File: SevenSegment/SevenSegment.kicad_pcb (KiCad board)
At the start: 2 copper layers, 28.5 x 42.7 mm, 11 parts, among them IC1 CD4033BE, IC2 CD4033BE, J1 Conn_01x04

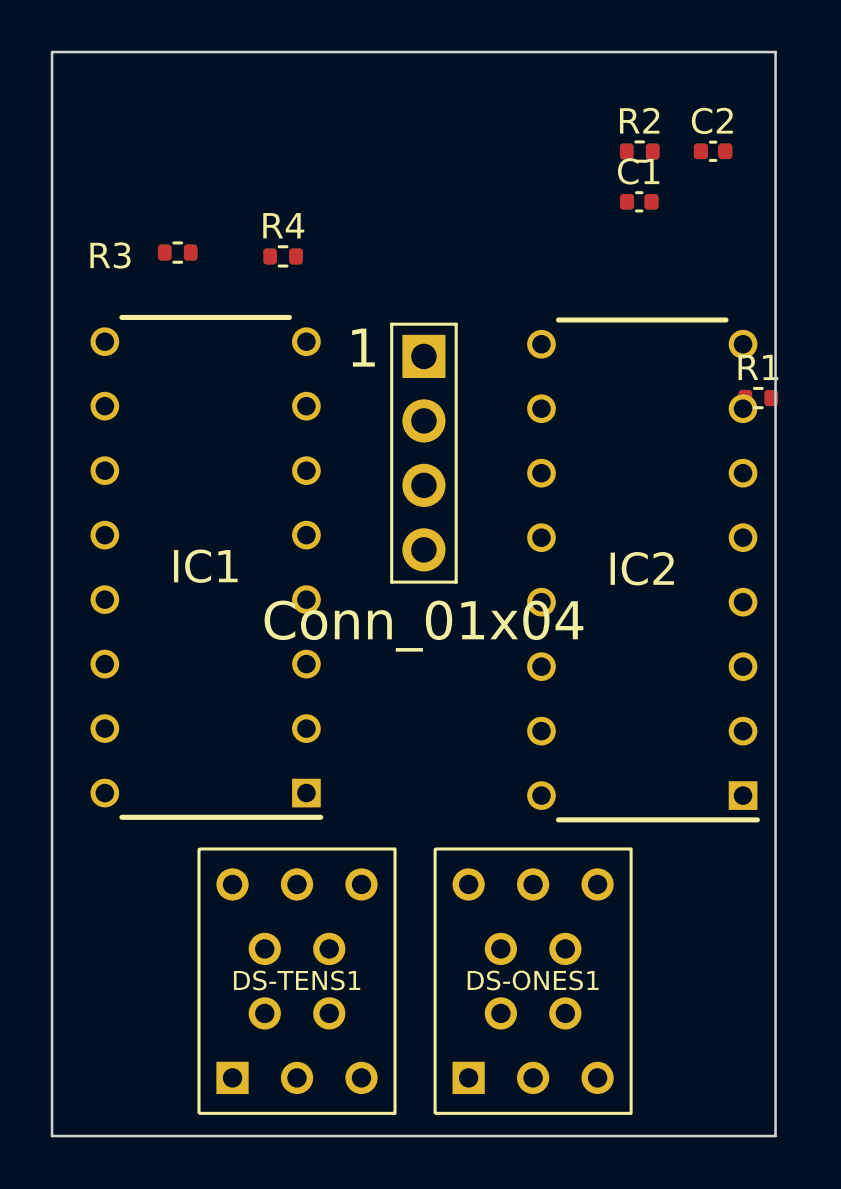
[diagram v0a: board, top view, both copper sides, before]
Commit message: Layout SevenSegment Board. Nano Schematic
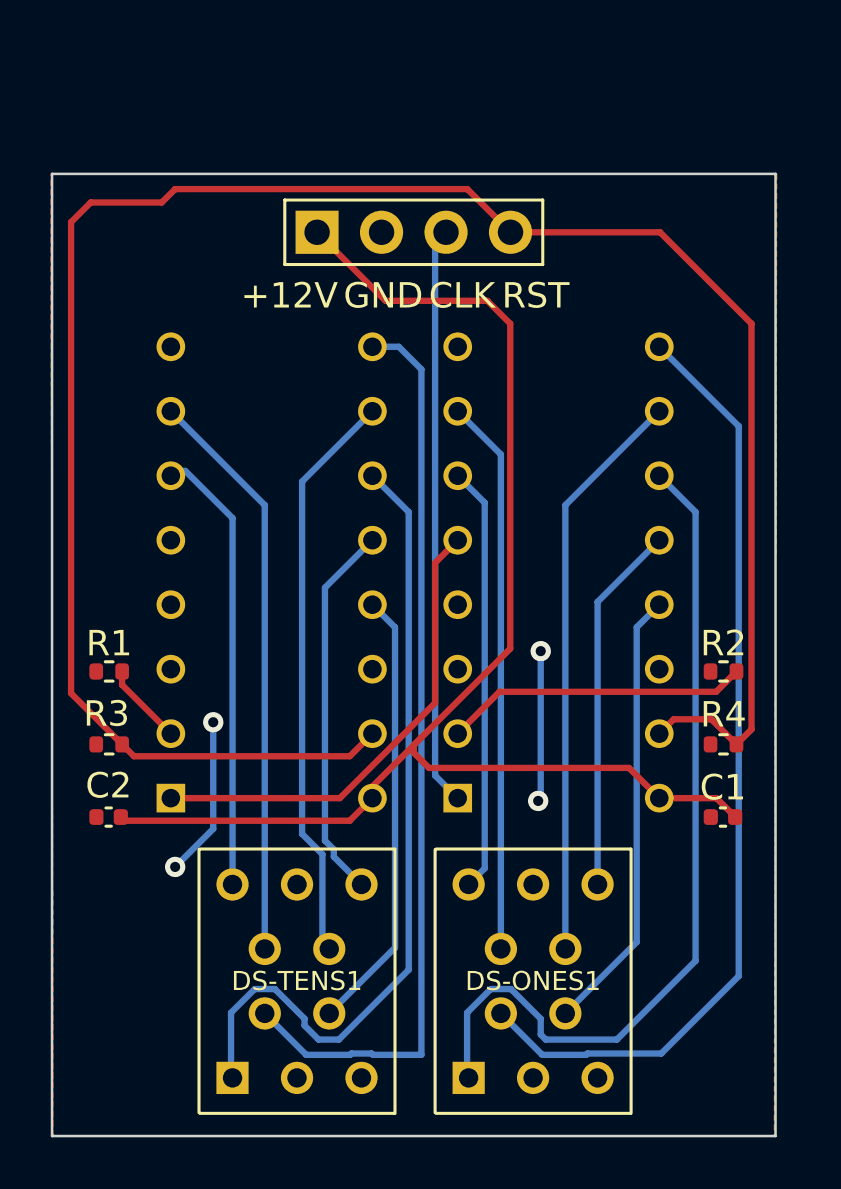
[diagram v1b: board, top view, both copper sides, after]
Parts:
- IC1, IC2: moved to B.Cu
- moved C2 35.4 mm to (92.2, 102.3)
- moved R1 27.7 mm to (92.2, 96.6), turned to 180 degrees
- moved R4 25.9 mm to (116.4, 99.5)
- moved C1 24.5 mm to (116.4, 102.3)
- moved R2 20.7 mm to (116.4, 96.6), turned to 180 degrees
- moved R3 19.6 mm to (92.2, 99.5)
- moved J1 8.71 mm to (104.2, 79.3), turned to 90 degrees
- moved IC2 3.30 mm to (109.9, 92.7), turned to 0 degrees
- moved IC1 2.61 mm to (98.6, 92.7), turned to 0 degrees
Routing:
- net /RESET: track 0.00 -> 81.9 mm
- net +12V: track 0.00 -> 54.7 mm
- net /D1: track 0.00 -> 37.4 mm
- net /D2: track 0.00 -> 36.2 mm
- net /E1: track 0.00 -> 34.3 mm
- net /E2: track 0.00 -> 32.3 mm
- net CLOCK_BAR: track 0.00 -> 22.8 mm
- net /A2: track 0.00 -> 22.8 mm
- net /G2: track 0.00 -> 22.7 mm
- net /A1: track 0.00 -> 22.7 mm
- net /G1: track 0.00 -> 21.9 mm
- net CARRY_1: track 0.00 -> 18.7 mm
- net /F2: track 0.00 -> 17.7 mm
- net /C1: track 0.00 -> 17.6 mm
- net /C2: track 0.00 -> 17.5 mm
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- added copper zone on F.Cu, net GND
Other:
- board size 28.5 x 42.7 mm -> 28.5 x 37.9 mm
- board text added: "+12V"
- board text added: "CLK"
- board text added: "GND"
- board text added: "RST"
- board text added: "SevenSegment v0.0"

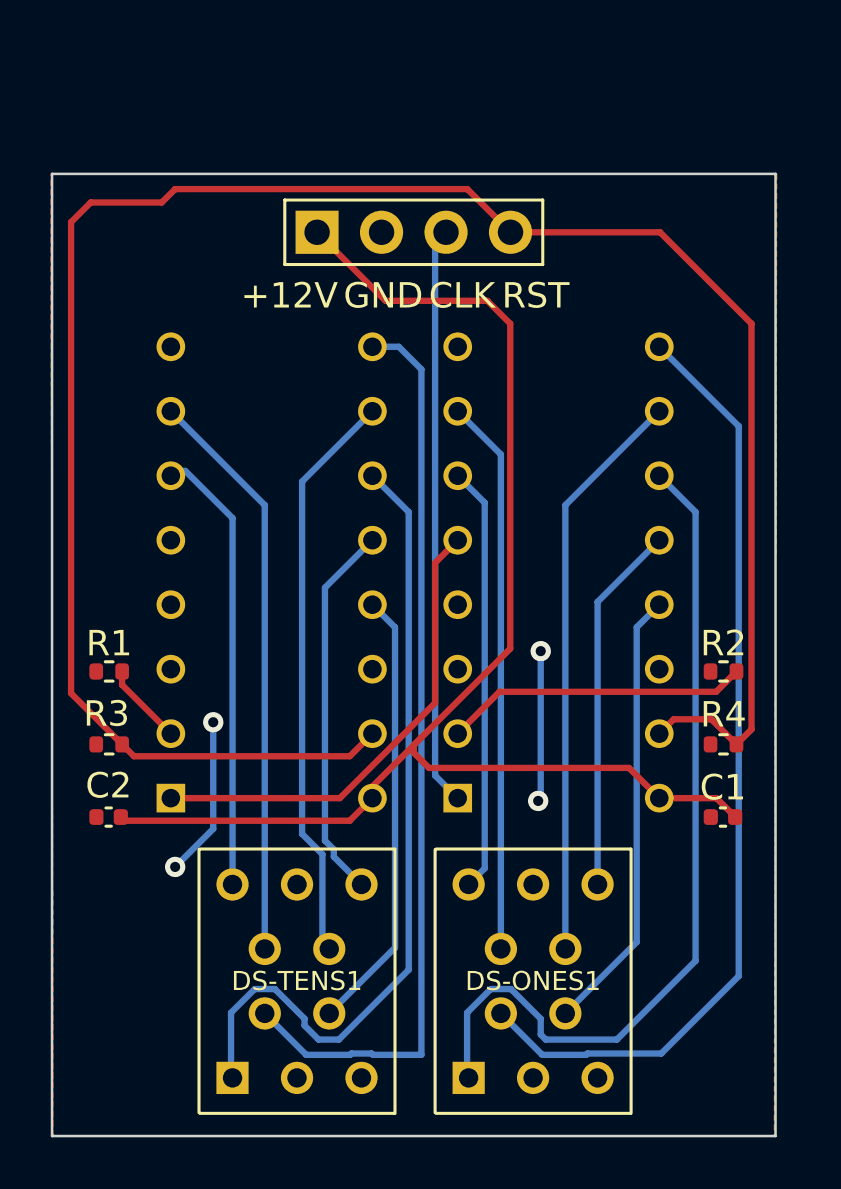
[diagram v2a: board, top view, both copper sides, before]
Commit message: SevenSegment PCB v1.0
Push TDSR0706's together, move header pins, add more header pins for mechanical stability, make board less wide, rounded tracks, moved ICs to top of board for better clearance.
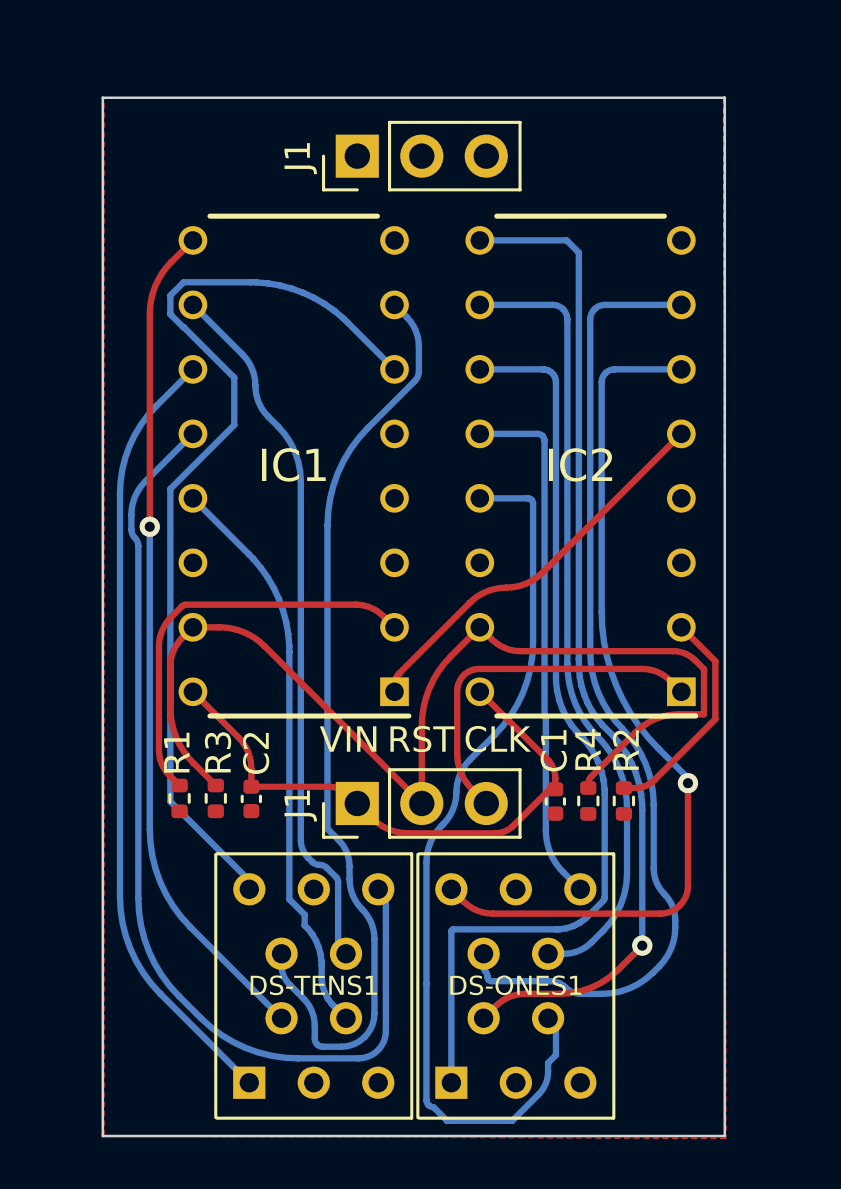
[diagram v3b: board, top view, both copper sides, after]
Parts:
- added J1: Conn_01x04, Connector_PinHeader_2.54mm:PinHeader_1x03_P2.54mm_Vertical, F.Cu at (102.0, 76.3)
- IC1, IC2: moved to F.Cu
- J1: footprint 4ms_Connector:Pins_1x04_2.54mm_TH_SWD -> Connector_PinHeader_2.54mm:PinHeader_1x03_P2.54mm_Vertical
- moved J1 22.6 mm to (102.0, 101.8)
- moved C1 6.63 mm to (109.8, 101.7), turned to 90 degrees
- moved R2 6.44 mm to (112.5, 101.7), turned to -90 degrees
- moved R4 5.77 mm to (111.1, 101.7), turned to 90 degrees
- moved R1 5.72 mm to (95.0, 101.6), turned to -90 degrees
- moved C2 5.67 mm to (97.8, 101.6), turned to 90 degrees
- moved R3 4.71 mm to (96.4, 101.6), turned to 90 degrees
- moved IC1 4.28 mm to (99.5, 88.5), turned to 180 degrees
- moved IC2 4.28 mm to (110.8, 88.5), turned to 180 degrees
- moved DS-ONES1 0.71 mm to (110.8, 105.2)
- moved DS-TENS1 0.69 mm to (102.8, 105.2)
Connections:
- J1 pad 2: GND -> /RESET
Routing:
- net /RESET: track 81.9 -> 43.6 mm
- net +12V: track 54.7 -> 22.8 mm
- net /B2: track 14.9 -> 38.7 mm
- net /F2: track 17.7 -> 37.0 mm
- net /C1: track 17.6 -> 35.5 mm
- net /F1: track 16.8 -> 34.5 mm, vias 0 -> 1
- net /G1: track 21.9 -> 38.6 mm
- net /G2: track 22.7 -> 37.0 mm
- net Net-(IC1-Pad2): track 3.25 -> 16.3 mm
- net GND: track 12.3 -> 0.00 mm, vias 4 -> 0
- net /A1: track 22.7 -> 31.1 mm
- net CLOCK_BAR: track 22.8 -> 14.4 mm
- net /B1: track 14.6 -> 20.8 mm
- net /A2: track 22.8 -> 27.8 mm
- net /C2: track 17.5 -> 22.6 mm
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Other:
- board size 28.5 x 37.9 mm -> 24.5 x 40.9 mm
- board text added: "SevenSegment v1.0"
- board text added: "VIN"
- board text removed: "+12V"
- board text removed: "GND"
- board text removed: "SevenSegment v0.0"

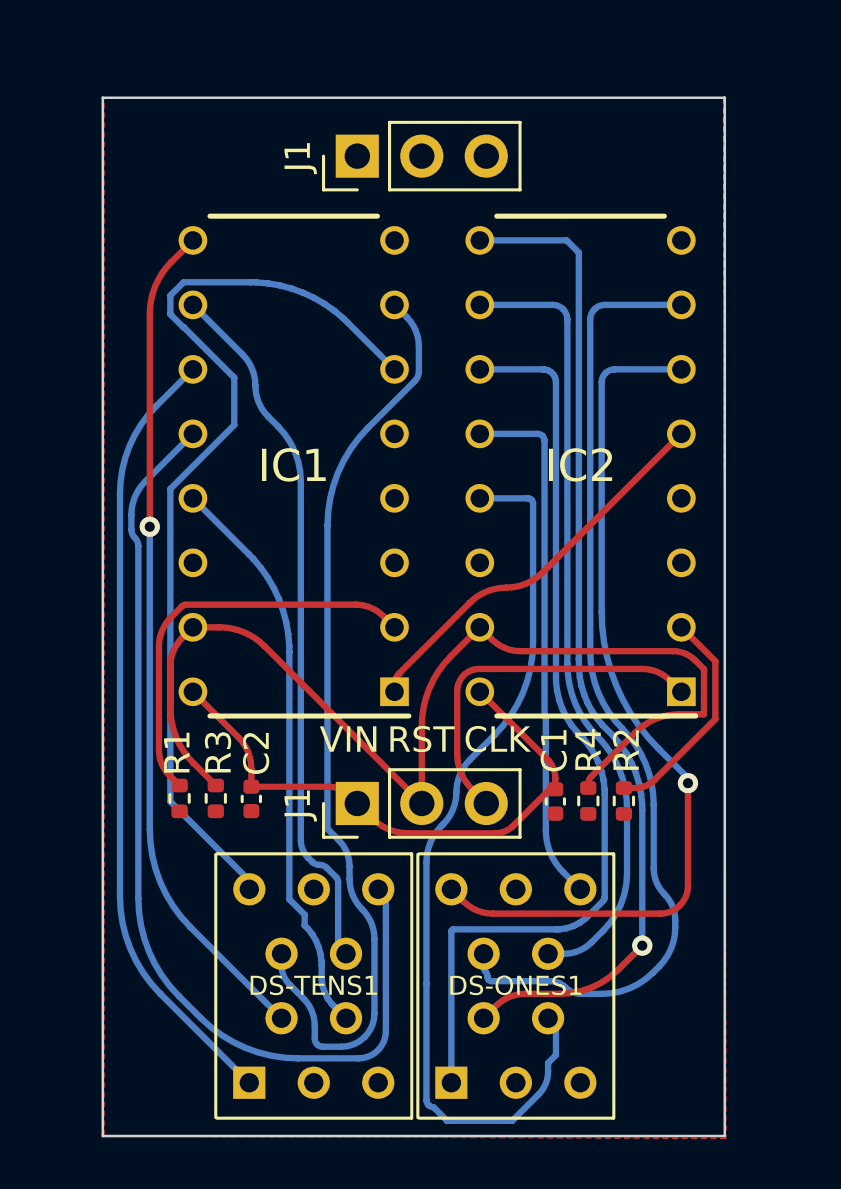
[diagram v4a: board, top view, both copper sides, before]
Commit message: Add startup led flashing to firmware.
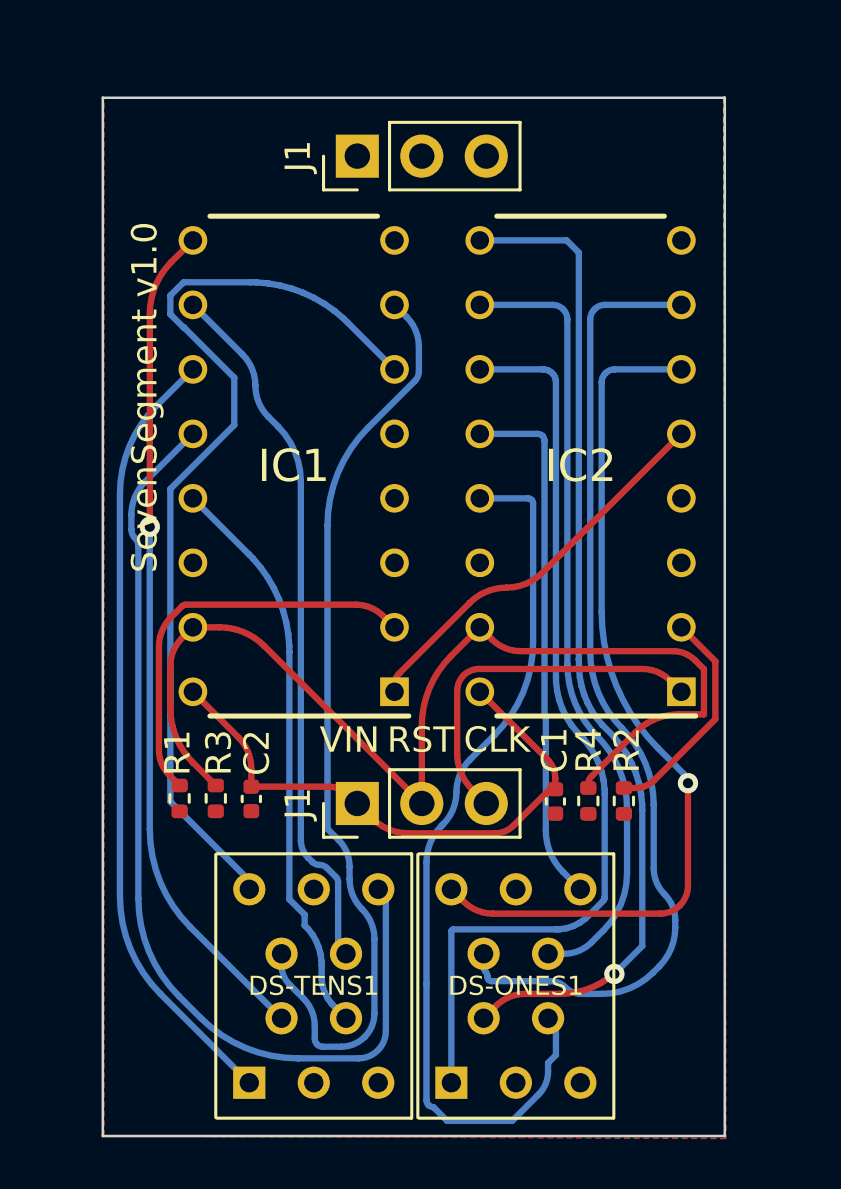
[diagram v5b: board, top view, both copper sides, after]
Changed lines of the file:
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@@
   (gr_rect (start 92 74) (end 116.5 114.9)
     (stroke (width 0.15) (type default)) (fill none) (layer "User.4"))
-  (gr_text "SevenSegment v1.0" (at 93.6 85.8 -270) (layer "B.SilkS")
-    (effects (font (size 1 1) (thickness 0.15)))
-  )
   (gr_text "RST\n" (at 104.475 99.3) (layer "F.SilkS")
     (effects (font (size 1 1) (thickness 0.15)))
@@
   )
   (gr_text "CLK" (at 107.475 99.3) (layer "F.SilkS")
+    (effects (font (size 1 1) (thickness 0.15)))
+  )
+  (gr_text "SevenSegment v1.0" (at 93.6 85.8 90) (layer "F.SilkS")
     (effects (font (size 1 1) (thickness 0.15)))
   )
@@
   (arc (start 110.183604 109.05) (mid 110.460516 109.235027) (end 110.787157 109.3) (width 0.25) (layer "B.Cu") (net 21))
   (arc (start 113.65 104.348959) (mid 113.760453 104.904248) (end 114.075 105.375) (width 0.25) (layer "B.Cu") (net 21))
-  (segment (start 113.2 107.4) (end 112.25 108.35) (width 0.25) (layer "F.Cu") (net 22))
-  (segment (start 109.956497 109.3) (end 108.588822 109.3) (width 0.25) (layer "F.Cu") (net 22))
+  (segment (start 112.102002 108.515408) (end 112.023617 108.515408) (width 0.25) (layer "F.Cu") (net 22))
+  (segment (start 112.023617 108.515408) (end 111.835011 108.704014) (width 0.25) (layer "F.Cu") (net 22))
   (segment (start 107.43 109.78) (end 106.95 110.26) (width 0.25) (layer "F.Cu") (net 22))
-  (via (at 113.2 107.4) (size 0.8) (drill 0.4) (layers "F.Cu" "B.Cu") (net 22))
+  (segment (start 109.951813 109.3) (end 108.588822 109.3) (width 0.25) (layer "F.Cu") (net 22))
+  (via (at 112.102002 108.515408) (size 0.8) (drill 0.4) (layers "F.Cu" "B.Cu") (net 22))
+  (arc (start 111.835011 108.704014) (mid 110.939505 109.147428) (end 109.951813 109.3) (width 0.25) (layer "F.Cu") (net 22))
   (arc (start 108.588822 109.3) (mid 107.961672 109.424747) (end 107.43 109.78) (width 0.25) (layer "F.Cu") (net 22))
-  (arc (start 112.25 108.35) (mid 111.197731 109.053103) (end 109.956497 109.3) (width 0.25) (layer "F.Cu") (net 22))
+  (segment (start 113.197504 101.849039) (end 113.156425 101.431979) (width 0.25) (layer "B.Cu") (net 22))
+  (segment (start 113.074666 101.020953) (end 112.953013 100.619921) (width 0.25) (layer "B.Cu") (net 22))
+  (segment (start 112.096398 99.190747) (end 112.096398 99.177197) (width 0.25) (layer "B.Cu") (net 22))
+  (segment (start 113.2 107.41741) (end 113.2 102.058578) (width 0.25) (layer "B.Cu") (net 22))
+  (segment (start 110.7 80.09799) (end 110.22201 79.62) (width 0.25) (layer "B.Cu") (net 22))
+  (segment (start 112.792638 100.232743) (end 112.595086 99.86315) (width 0.25) (layer "B.Cu") (net 22))
+  (segment (start 110.22201 79.62) (end 106.8 79.62) (width 0.25) (layer "B.Cu") (net 22))
+  (segment (start 110.741572 96.837671) (end 110.707076 96.487425) (width 0.25) (layer "B.Cu") (net 22))
+  (segment (start 112.362258 99.514699) (end 112.096398 99.190747) (width 0.25) (layer "B.Cu") (net 22))
+  (segment (start 112.953013 100.619921) (end 112.792638 100.232743) (width 0.25) (layer "B.Cu") (net 22))
+  (segment (start 111.403375 98.435391) (end 111.209349 98.14501) (width 0.25) (layer "B.Cu") (net 22))
+  (segment (start 110.809701 97.180177) (end 110.741572 96.837671) (width 0.25) (layer "B.Cu") (net 22))
+  (segment (start 110.7 96.118982) (end 110.7 80.09799) (width 0.25) (layer "B.Cu") (net 22))
+  (segment (start 112.096398 99.177197) (end 111.626642 98.707441) (width 0.25) (layer "B.Cu") (net 22))
   (segment (start 112.595086 99.86315) (end 112.362258 99.514699) (width 0.25) (layer "B.Cu") (net 22))
-  (segment (start 111.626642 98.707441) (end 111.403375 98.435391) (width 0.25) (layer "B.Cu") (net 22))
-  (segment (start 110.809701 97.180177) (end 110.741572 96.837671) (width 0.25) (layer "B.Cu") (net 22))
-  (segment (start 110.741572 96.837671) (end 110.707076 96.487425) (width 0.25) (layer "B.Cu") (net 22))
-  (segment (start 113.074666 101.020953) (end 112.953013 100.619921) (width 0.25) (layer "B.Cu") (net 22))
-  (segment (start 110.7 96.118982) (end 110.7 80.09799) (width 0.25) (layer "B.Cu") (net 22))
-  (segment (start 111.209349 98.14501) (end 111.044726 97.837023) (width 0.25) (layer "B.Cu") (net 22))
-  (segment (start 110.702728 96.121646) (end 110.7 96.118982) (width 0.25) (layer "B.Cu") (net 22))
-  (segment (start 111.403375 98.435391) (end 111.209349 98.14501) (width 0.25) (layer "B.Cu") (net 22))
   (segment (start 111.044726 97.837023) (end 110.911081 97.514379) (width 0.25) (layer "B.Cu") (net 22))
   (segment (start 113.156425 101.431979) (end 113.074666 101.020953) (width 0.25) (layer "B.Cu") (net 22))
-  (segment (start 113.2 107.4) (end 113.2 102.058578) (width 0.25) (layer "B.Cu") (net 22))
+  (segment (start 113.2 102.058578) (end 113.197504 101.849039) (width 0.25) (layer "B.Cu") (net 22))
   (segment (start 110.911081 97.514379) (end 110.809701 97.180177) (width 0.25) (layer "B.Cu") (net 22))
-  (segment (start 112.096398 99.190747) (end 112.096398 99.177197) (width 0.25) (layer "B.Cu") (net 22))
-  (segment (start 110.22201 79.62) (end 106.8 79.62) (width 0.25) (layer "B.Cu") (net 22))
-  (segment (start 112.362258 99.514699) (end 112.096398 99.190747) (width 0.25) (layer "B.Cu") (net 22))
-  (segment (start 110.7 80.09799) (end 110.22201 79.62) (width 0.25) (layer "B.Cu") (net 22))
-  (segment (start 112.792638 100.232743) (end 112.595086 99.86315) (width 0.25) (layer "B.Cu") (net 22))
-  (segment (start 112.953013 100.619921) (end 112.792638 100.232743) (width 0.25) (layer "B.Cu") (net 22))
-  (segment (start 113.197504 101.849039) (end 113.156425 101.431979) (width 0.25) (layer "B.Cu") (net 22))
-  (segment (start 113.2 102.058578) (end 113.197504 101.849039) (width 0.25) (layer "B.Cu") (net 22))
+  (segment (start 112.102002 108.515408) (end 113.2 107.41741) (width 0.25) (layer "B.Cu") (net 22))
+  (segment (start 111.626642 98.707441) (end 111.403375 98.435391) (width 0.25) (layer "B.Cu") (net 22))
   (segment (start 110.707076 96.487425) (end 110.702728 96.121646) (width 0.25) (layer "B.Cu") (net 22))
-  (segment (start 112.096398 99.177197) (end 111.626642 98.707441) (width 0.25) (layer "B.Cu") (net 22))
+  (segment (start 110.702728 96.121646) (end 110.7 96.118982) (width 0.25) (layer "B.Cu") (net 22))
+  (segment (start 111.209349 98.14501) (end 111.044726 97.837023) (width 0.25) (layer "B.Cu") (net 22))
   (segment (start 110.25 96.315507) (end 110.25 82.740416) (width 0.25) (layer "B.Cu") (net 23))
   (segment (start 112.6 104.561852) (end 112.6 101.988908) (width 0.25) (layer "B.Cu") (net 23))
